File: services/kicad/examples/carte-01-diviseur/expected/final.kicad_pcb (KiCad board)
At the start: 2 copper layers, 20 x 14.5 mm, 5 parts, among them J1 IN

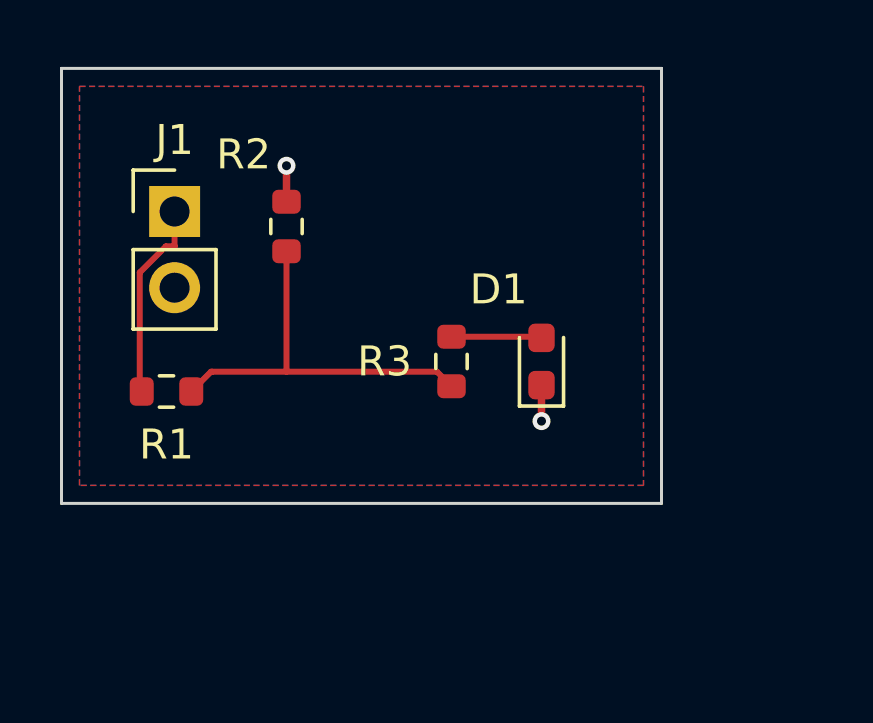
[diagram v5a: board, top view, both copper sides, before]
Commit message: feat(placement): les peripheriques se REPARTISSENT, ils ne s empilent plus
Question de l utilisateur devant le rendu : « c est quoi ce type de placement ? ».
Les composants s entassaient d un seul cote du boitier, etiquettes de
serigraphie l une sur l autre, trois quarts de la couronne vides.

TROIS CAUSES, toutes dans `_poser_les_peripheriques`, toutes la meme faute —
un angle unique pour tout un groupe :

  - les DIRECTS qui visent la meme broche (tous les decouplages d un rail,
    toutes les resistances d un meme signal) recevaient le MEME `angle_vers`
    et le meme rayon de depart ;
  - les SUIVEURS d un meme parent recevaient tous atan2(parent - centre) ;
  - les ISOLES partaient tous de l angle 0.0, c est-a-dire du meme point.

`le_long_du_rayon` ne s ecartait qu une fois la place prise : d ou la file.

REMEDE : `_ecart_en_eventail`. Le PREMIER de chaque groupe garde EXACTEMENT la
direction calculee — c est la topologie, on ne la perd pas pour faire joli — et
les suivants s ecartent symetriquement de 3 x `_PAS_ANGLE_DEG`.
Rien de deja pose ne bouge : seul l ANGLE DE DEPART de la recherche change, et
`le_long_du_rayon` reste seul juge de ce qui est libre.

BANC DES DIX CARTES, contour resserre ET peripheriques repartis :

    carte             demandee    livree         err  manq
    carte-01           25 x 20    20,1 x 13,6     0    0
    carte-02           55 x 40    34,9 x 25,2     0    0
    carte-03           50 x 35    27,6 x 19,9     0    0
    carte-04           60 x 45    36,6 x 29,8     0    0
    carte-05           70 x 50    40,0 x 32,6     0    0
    carte-06           80 x 60    46,5 x 36,4     0    0
    carte-07          110 x 80    47,7 x 38,8     0    0
    carte-08          125 x 95    57,4 x 44,1     0    0
    carte-09          130 x 100   57,8 x 45,2     0    0
    carte-10          140 x 105   59,0 x 45,8     0    0

Dix sur dix, 100 % route. carte-07 gagne 5,5 mm de largeur sur le passage
precedent, carte-06 deux, carte-10 deux. Sur ca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
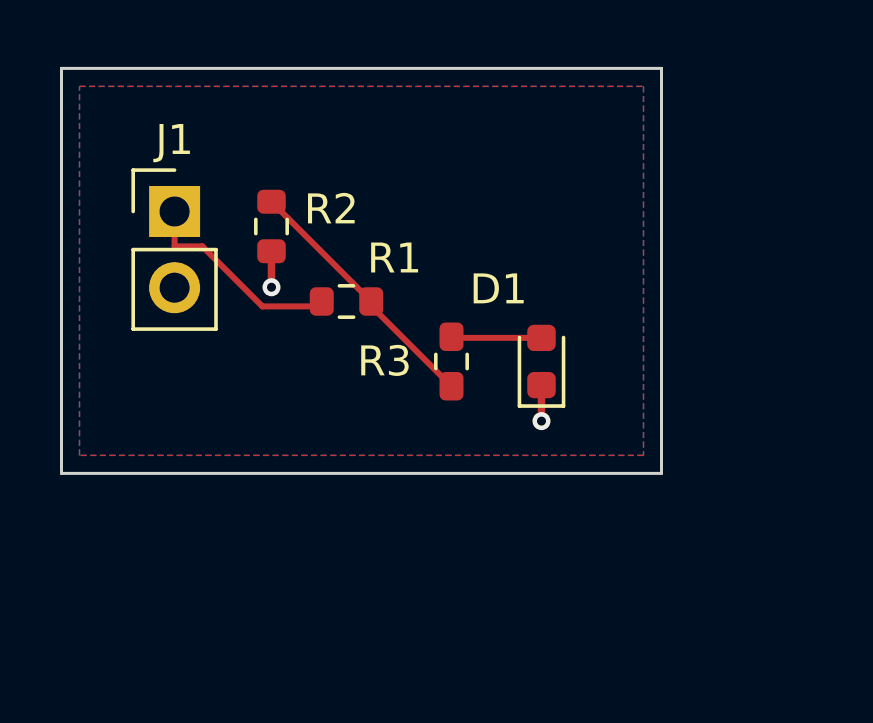
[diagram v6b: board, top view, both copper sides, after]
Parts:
- moved R1 6.71 mm to (145.5, 103.0)
- moved R2 0.50 mm to (143.0, 100.5), turned to -90 degrees
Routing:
- net MID: track 13.2 -> 8.64 mm
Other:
- board size 20 x 14.5 mm -> 20 x 13.5 mm

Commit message: docs(banc): les dix boards du banc du 2026-09-23, service corrige
Artefacts du banc dont le tableau est deja commite : les dix cartes a
100 % route, 0 erreur, 0 connexion manquante, chacune a la taille de son
circuit.

Co-Authored-By: Claude Opus 5 <noreply@anthropic.com>
Claude-Session: https://claude.ai/code/session_01TnMqm4La2CxQHHB5K8aSSV
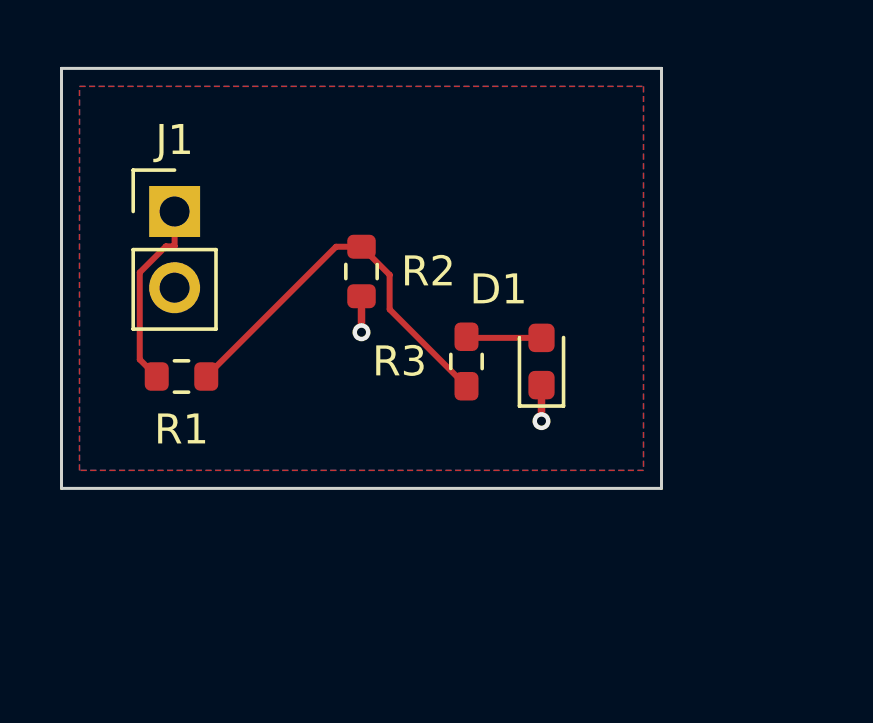
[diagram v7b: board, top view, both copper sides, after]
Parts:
- moved R1 6.04 mm to (140.0, 105.5)
- moved R2 3.35 mm to (146.0, 102.0)
- moved R3 0.50 mm to (149.5, 105.0)
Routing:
- net MID: track 8.64 -> 13.1 mm
- net VIN: track 6.96 -> 6.39 mm
- net LED_A: track 3.02 -> 2.52 mm
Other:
- board size 20 x 13.5 mm -> 20 x 14 mm
